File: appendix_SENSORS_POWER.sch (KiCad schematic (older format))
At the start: 49 parts, among them J401 Conn_01x02, J402 Conn_01x02, J403 Screw_Terminal_01x02, J404 Conn_01x02, J405 Conn_01x02, J406 Screw_Terminal_01x02, J407 Conn_01x02, J408 Conn_01x02, J409 Conn_01x02, J410 Conn_01x02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

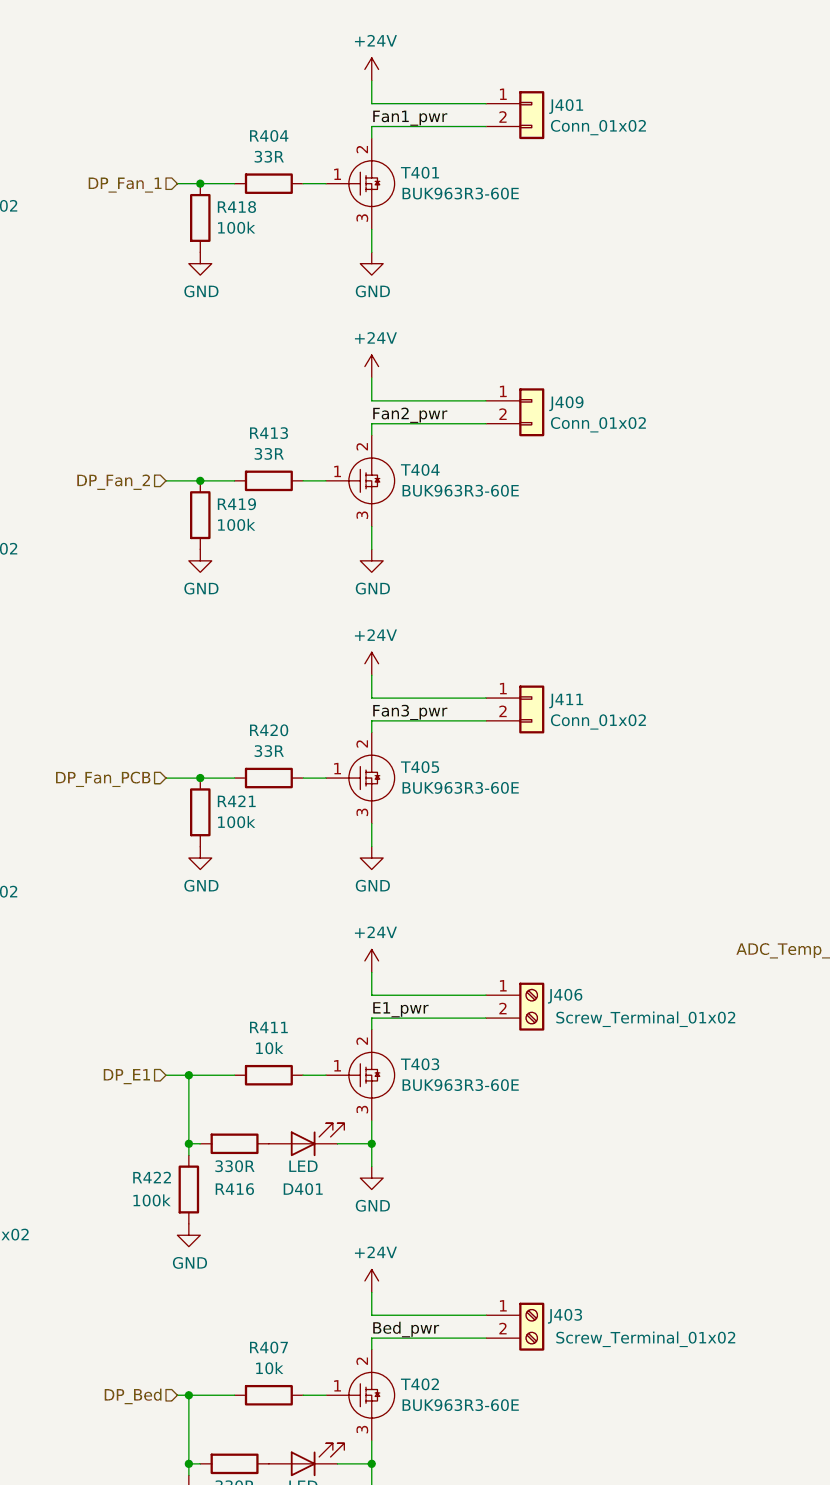
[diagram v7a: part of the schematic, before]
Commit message: added FT2232 by Marco M
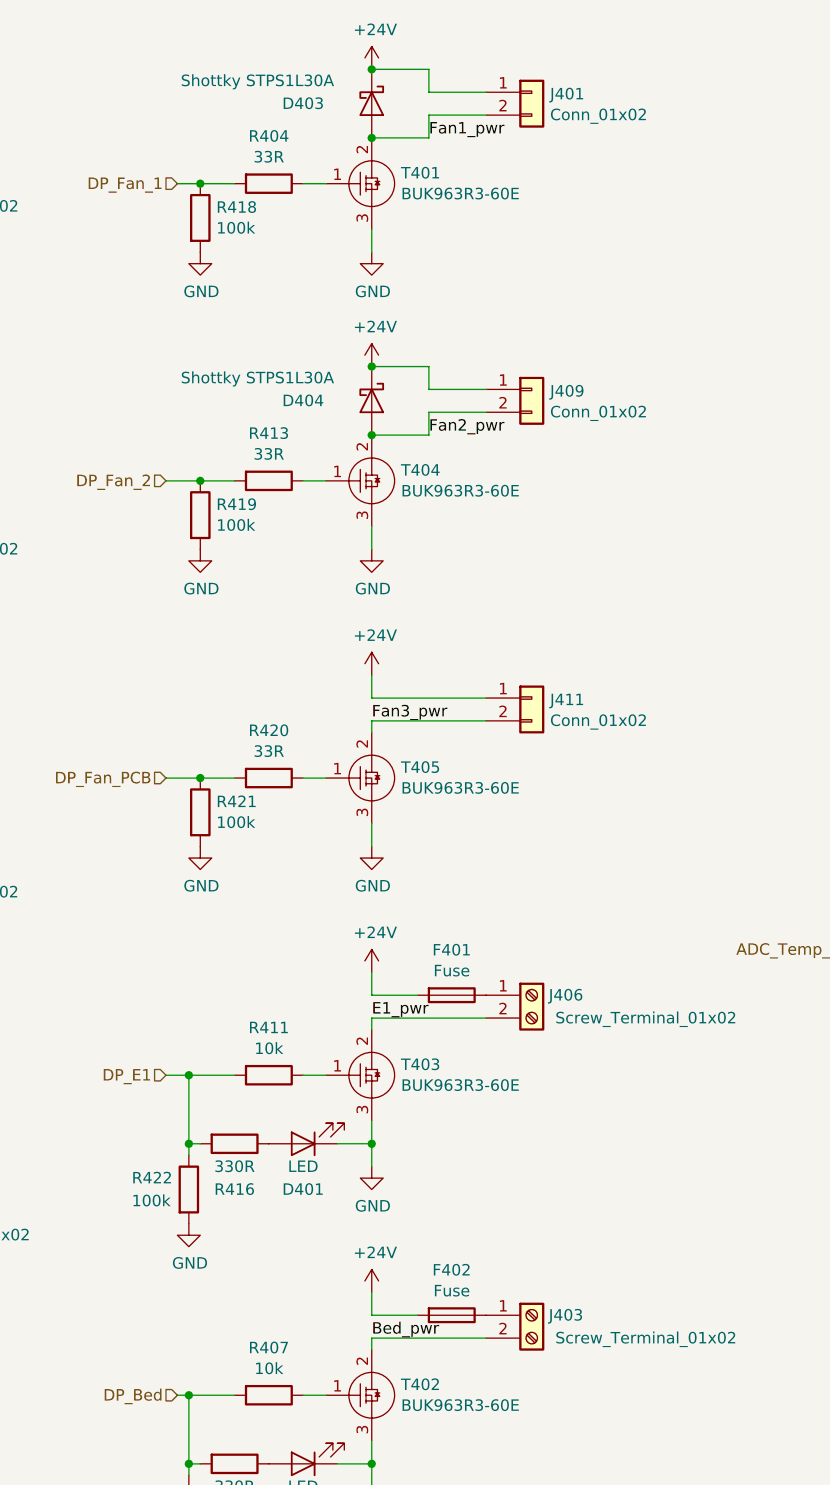
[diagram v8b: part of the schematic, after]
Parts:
- added D403, D404: Shottky STPS1L30A, Diodes_SMD:D_SMB, symbol Device:D_Schottky
- added F401, F402: Fuse, Fuse:Fuseholder_Blade_ATO_Littelfuse_Pudenz_2_Pin, symbol Device:Fuse
- C401, C402, C403, C404, C405, C406, C407: footprint Capacitors_SMD:C_0603 -> Capacitors_SMD:C_1210
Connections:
- net +24V: now also D403.1 (K), D404.1 (K), F401.2, F402.2; no longer J403.1 (Pin_1), J406.1 (Pin_1)
- net Fan1_pwr: now also D403.2 (A)
- net Fan2_pwr: now also D404.2 (A)
- new net: F401.1, J406.1 (Pin_1)
- new net: F402.1, J403.1 (Pin_1)
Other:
- moved on the sheet: J401
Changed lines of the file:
@@
 F 0 "C402" H 2165 1846 50  0000 L CNN
 F 1 "10u" H 2165 1755 50  0000 L CNN
-F 2 "Capacitors_SMD:C_0603" H 2088 1650 50  0001 C CNN
+F 2 "Capacitors_SMD:C_1210" H 2088 1650 50  0001 C CNN
 F 3 "~" H 2050 1800 50  0001 C CNN
 	1    2050 1800
@@
 Text HLabel 3900 1550 0    50   Input ~ 0
 DP_Fan_1
-Wire Wire Line
-	4750 1350 4750 1300
-Wire Wire Line
-	4750 1300 5250 1300
-Wire Wire Line
-	5250 1200 4750 1200
-Wire Wire Line
-	4750 1200 4750 1100
 $Comp
 L FHNW-Pro4E-FS19T8-Library:BUK963R3-60E T402
@@
 	4750 6600 5250 6600
 Wire Wire Line
-	5250 6500 4750 6500
-Wire Wire Line
 	4750 6500 4750 6400
 $Comp
@@
 Wire Wire Line
 	4750 5200 5250 5200
-Wire Wire Line
-	5250 5100 4750 5100
-Wire Wire Line
-	4750 5100 4750 5000
 Text HLabel 3900 6850 0    50   Input ~ 0
 DP_Bed
@@
 F 0 "C405" H 2165 6346 50  0000 L CNN
 F 1 "10u" H 2165 6255 50  0000 L CNN
-F 2 "Capacitors_SMD:C_0603" H 2088 6150 50  0001 C CNN
+F 2 "Capacitors_SMD:C_1210" H 2088 6150 50  0001 C CNN
 F 3 "~" H 2050 6300 50  0001 C CNN
 	1    2050 6300
@@
 F 0 "C403" H 8365 3396 50  0000 L CNN
 F 1 "10u" H 8365 3305 50  0000 L CNN
-F 2 "Capacitors_SMD:C_0603" H 8288 3200 50  0001 C CNN
+F 2 "Capacitors_SMD:C_1210" H 8288 3200 50  0001 C CNN
 F 3 "~" H 8250 3350 50  0001 C CNN
 	1    8250 3350
@@
 F 0 "C401" H 8365 1896 50  0000 L CNN
 F 1 "10u" H 8365 1805 50  0000 L CNN
-F 2 "Capacitors_SMD:C_0603" H 8288 1700 50  0001 C CNN
+F 2 "Capacitors_SMD:C_1210" H 8288 1700 50  0001 C CNN
 F 3 "~" H 8250 1850 50  0001 C CNN
 	1    8250 1850
@@
 F 0 "C404" H 2165 3346 50  0000 L CNN
 F 1 "10u" H 2165 3255 50  0000 L CNN
-F 2 "Capacitors_SMD:C_0603" H 2088 3150 50  0001 C CNN
+F 2 "Capacitors_SMD:C_1210" H 2088 3150 50  0001 C CNN
 F 3 "~" H 2050 3300 50  0001 C CNN
 	1    2050 3300
@@
 F 0 "C406" H 2165 4846 50  0000 L CNN
 F 1 "10u" H 2165 4755 50  0000 L CNN
-F 2 "Capacitors_SMD:C_0603" H 2088 4650 50  0001 C CNN
+F 2 "Capacitors_SMD:C_1210" H 2088 4650 50  0001 C CNN
 F 3 "~" H 2050 4800 50  0001 C CNN
 	1    2050 4800
@@
 L Connector_Generic:Conn_01x02 J401
 U 1 1 5CDCB859
-P 5450 1200
-F 0 "J401" H 5530 1192 50  0000 L CNN
-F 1 "Conn_01x02" H 5530 1101 50  0000 L CNN
-F 2 "Connectors_JST:JST_EH_B02B-EH-A_02x2.50mm_Straight" H 5450 1200 50  0001 C CNN
-F 3 "~" H 5450 1200 50  0001 C CNN
-	1    5450 1200
+P 5450 1150
+F 0 "J401" H 5530 1142 50  0000 L CNN
+F 1 "Conn_01x02" H 5530 1051 50  0000 L CNN
+F 2 "Connectors_JST:JST_EH_B02B-EH-A_02x2.50mm_Straight" H 5450 1150 50  0001 C CNN
+F 3 "~" H 5450 1150 50  0001 C CNN
+	1    5450 1150
 	1    0    0    -1
 $EndComp
@@
 L power:+24V #PWR0401
 U 1 1 5CDE05D1
-P 4750 1100
-F 0 "#PWR0401" H 4750 950 50  0001 C CNN
-F 1 "+24V" H 4765 1273 50  0000 C CNN
-F 2 "" H 4750 1100 50  0001 C CNN
-F 3 "" H 4750 1100 50  0001 C CNN
-	1    4750 1100
+P 4750 1050
+F 0 "#PWR0401" H 4750 900 50  0001 C CNN
+F 1 "+24V" H 4765 1223 50  0000 C CNN
+F 2 "" H 4750 1050 50  0001 C CNN
+F 3 "" H 4750 1050 50  0001 C CNN
+	1    4750 1050
 	1    0    0    -1
 $EndComp
@@
 Text HLabel 3850 2850 0    50   Input ~ 0
 DP_Fan_2
-Wire Wire Line
-	4750 2650 4750 2600
-Wire Wire Line
-	4750 2600 5250 2600
-Wire Wire Line
-	5250 2500 4750 2500
-Wire Wire Line
-	4750 2500 4750 2400
-$Comp
-L Connector_Generic:Conn_01x02 J409
-U 1 1 5CDE31D7
-P 5450 2500
-F 0 "J409" H 5530 2492 50  0000 L CNN
-F 1 "Conn_01x02" H 5530 2401 50  0000 L CNN
-F 2 "Connectors_JST:JST_EH_B02B-EH-A_02x2.50mm_Straight" H 5450 2500 50  0001 C CNN
-F 3 "~" H 5450 2500 50  0001 C CNN
-	1    5450 2500
-	1    0    0    -1
-$EndComp
-$Comp
-L power:+24V #PWR0409
-U 1 1 5CDE31E1
-P 4750 2400
-F 0 "#PWR0409" H 4750 2250 50  0001 C CNN
-F 1 "+24V" H 4765 2573 50  0000 C CNN
-F 2 "" H 4750 2400 50  0001 C CNN
-F 3 "" H 4750 2400 50  0001 C CNN
-	1    4750 2400
-	1    0    0    -1
-$EndComp
 $Comp
 L Device:R R414
@@
 Wire Wire Line
 	8250 1600 8650 1600
-Text Label 4750 2600 0    50   ~ 0
+Text Label 5000 2650 0    50   ~ 0
 Fan2_pwr
 Text Label 4750 5200 0    50   ~ 0
@@
 Text Label 4750 6600 0    50   ~ 0
 Bed_pwr
-Text Label 4750 1300 0    50   ~ 0
+Text Label 5000 1350 0    50   ~ 0
 Fan1_pwr
 $Bitmap
@@
 F 0 "C407" H 7415 5196 50  0000 L CNN
 F 1 "10u" H 7415 5105 50  0000 L CNN
-F 2 "Capacitors_SMD:C_0603" H 7338 5000 50  0001 C CNN
+F 2 "Capacitors_SMD:C_1210" H 7338 5000 50  0001 C CNN
 F 3 "~" H 7300 5150 50  0001 C CNN
 	1    7300 5150
@@
 	3950 7200 3950 7150
 Connection ~ 3950 7150
+$Comp
+L Device:Fuse F401
+U 1 1 5CB755BC
+P 5100 5100
+AR Path="/5CA39F21/5CB755BC" Ref="F401"  Part="1"
+AR Path="/5CB755BC" Ref="F?"  Part="1"
+F 0 "F401" V 4903 5100 50  0000 C CNN
+F 1 "Fuse" V 4994 5100 50  0000 C CNN
+F 2 "Fuse:Fuseholder_Blade_ATO_Littelfuse_Pudenz_2_Pin" V 5030 5100 50  0001 C CNN
+F 3 "~" H 5100 5100 50  0001 C CNN
+	1    5100 5100
+	0    1    1    0
+$EndComp
+Wire Wire Line
+	4950 5100 4750 5100
+Wire Wire Line
+	4750 5100 4750 5000
+$Comp
+L Device:Fuse F402
+U 1 1 5CB7E081
+P 5100 6500
+AR Path="/5CA39F21/5CB7E081" Ref="F402"  Part="1"
+AR Path="/5CB7E081" Ref="F?"  Part="1"
+F 0 "F402" V 4903 6500 50  0000 C CNN
+F 1 "Fuse" V 4994 6500 50  0000 C CNN
+F 2 "Fuse:Fuseholder_Blade_ATO_Littelfuse_Pudenz_2_Pin" V 5030 6500 50  0001 C CNN
+F 3 "~" H 5100 6500 50  0001 C CNN
+	1    5100 6500
+	0    1    1    0
+$EndComp
+Wire Wire Line
+	4950 6500 4750 6500
+$Comp
+L Device:D_Schottky D?
+U 1 1 5CB76565
+P 4750 1200
+AR Path="/5CB76565" Ref="D?"  Part="1"
+AR Path="/5CA39F21/5CB76565" Ref="D403"  Part="1"
+F 0 "D403" V 4750 900 50  0000 C CNN
+F 1 "Shottky STPS1L30A" V 4650 700 50  0000 C CNN
+F 2 "Diodes_SMD:D_SMB" H 4750 1200 50  0001 C CNN
+F 3 "~" H 4750 1200 50  0001 C CNN
+	1    4750 1200
+	0    1    1    0
+$EndComp
+Wire Wire Line
+	4750 1050 5000 1050
+Wire Wire Line
+	5000 1050 5000 1150
+Connection ~ 4750 1050
+Wire Wire Line
+	4750 1350 5000 1350
+Wire Wire Line
+	5000 1350 5000 1250
+Connection ~ 4750 1350
+Wire Wire Line
+	5000 1150 5250 1150
+Wire Wire Line
+	5000 1250 5250 1250
+$Comp
+L Connector_Generic:Conn_01x02 J409
+U 1 1 5CB907CD
+P 5450 2450
+F 0 "J409" H 5530 2442 50  0000 L CNN
+F 1 "Conn_01x02" H 5530 2351 50  0000 L CNN
+F 2 "Connectors_JST:JST_EH_B02B-EH-A_02x2.50mm_Straight" H 5450 2450 50  0001 C CNN
+F 3 "~" H 5450 2450 50  0001 C CNN
+	1    5450 2450
+	1    0    0    -1
+$EndComp
+$Comp
+L power:+24V #PWR0409
+U 1 1 5CB907D7
+P 4750 2350
+F 0 "#PWR0409" H 4750 2200 50  0001 C CNN
+F 1 "+24V" H 4765 2523 50  0000 C CNN
+F 2 "" H 4750 2350 50  0001 C CNN
+F 3 "" H 4750 2350 50  0001 C CNN
+	1    4750 2350
+	1    0    0    -1
+$EndComp
+$Comp
+L Device:D_Schottky D?
+U 1 1 5CB907E1
+P 4750 2500
+AR Path="/5CB907E1" Ref="D?"  Part="1"
+AR Path="/5CA39F21/5CB907E1" Ref="D404"  Part="1"
+F 0 "D404" V 4750 2200 50  0000 C CNN
+F 1 "Shottky STPS1L30A" V 4650 2000 50  0000 C CNN
+F 2 "Diodes_SMD:D_SMB" H 4750 2500 50  0001 C CNN
+F 3 "~" H 4750 2500 50  0001 C CNN
+	1    4750 2500
+	0    1    1    0
+$EndComp
+Wire Wire Line
+	4750 2350 5000 2350
+Wire Wire Line
+	5000 2350 5000 2450
+Connection ~ 4750 2350
+Wire Wire Line
+	5000 2650 5000 2550
+Wire Wire Line
+	5000 2450 5250 2450
+Wire Wire Line
+	5000 2550 5250 2550
+Wire Wire Line
+	5000 2650 4750 2650
+Connection ~ 4750 2650
 $EndSCHEMATC
